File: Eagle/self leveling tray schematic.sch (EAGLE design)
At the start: 9 parts

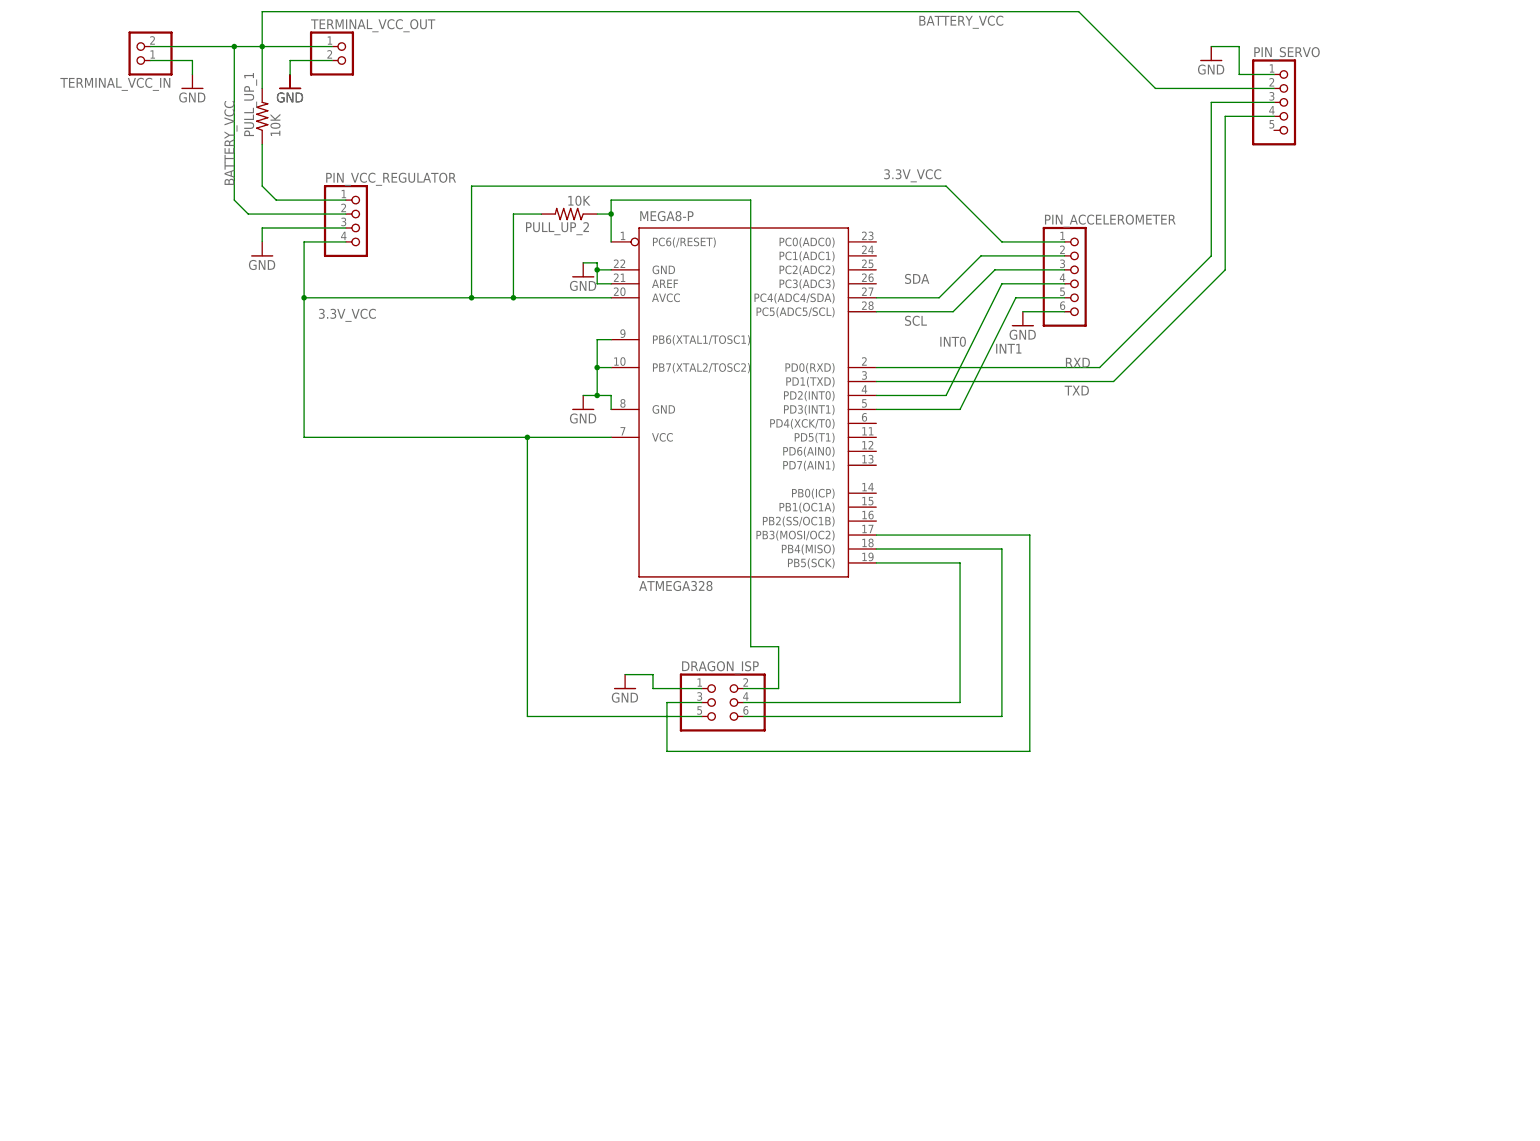
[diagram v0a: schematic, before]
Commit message: Schematic & Layout
Fixed ERC errors in schematic.
Created (practice?) layout.
Taylor Griffin
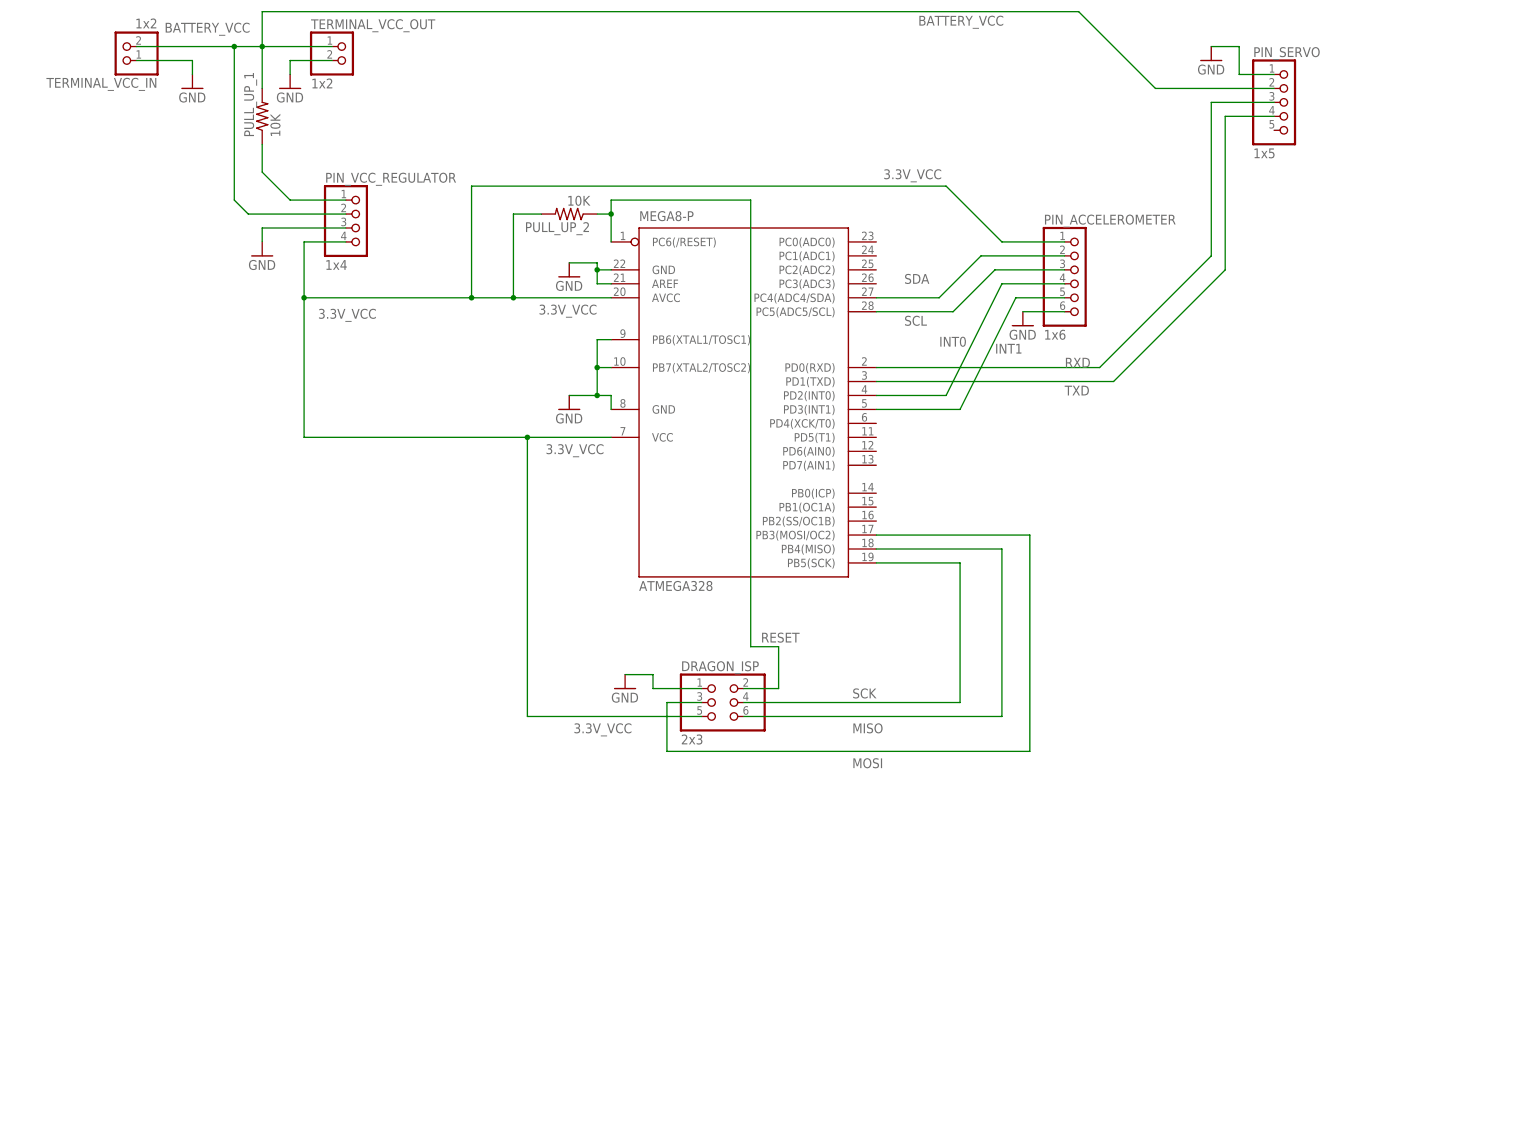
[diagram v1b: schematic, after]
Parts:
- DRAGON_ISP: value (none) -> 2x3
- PIN_ACCELEROMETER: value (none) -> 1x6
- PIN_SERVO: value (none) -> 1x5
- PIN_VCC_REGULATOR: value (none) -> 1x4
- TERMINAL_VCC_IN, TERMINAL_VCC_OUT: value (none) -> 1x2
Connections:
- net N$2 renamed MOSI
- net N$3 renamed MISO
- net N$4 renamed SCK
- net N$6 renamed RESET
- new net SHDN: PIN_VCC_REGULATOR.1, PULL_UP_1.1
- net BATTERY_VCC: no longer PIN_VCC_REGULATOR.1, PULL_UP_1.1
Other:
- moved on the sheet: TERMINAL_VCC_IN
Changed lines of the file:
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@@
 <part name="FRAME1" library="frames" deviceset="FRAME_A_L" device=""/>
 <part name="ATMEGA328" library="atmel" deviceset="MEGA8-P" device=""/>
-<part name="PIN_ACCELEROMETER" library="pinhead" deviceset="PINHD-1X6" device=""/>
-<part name="PIN_SERVO" library="pinhead" deviceset="PINHD-1X5" device=""/>
-<part name="PIN_VCC_REGULATOR" library="pinhead" deviceset="PINHD-1X4" device=""/>
-<part name="TERMINAL_VCC_IN" library="pinhead" deviceset="PINHD-1X2" device=""/>
-<part name="TERMINAL_VCC_OUT" library="pinhead" deviceset="PINHD-1X2" device=""/>
+<part name="PIN_ACCELEROMETER" library="pinhead" deviceset="PINHD-1X6" device="" value="1x6"/>
+<part name="PIN_SERVO" library="pinhead" deviceset="PINHD-1X5" device="" value="1x5"/>
+<part name="PIN_VCC_REGULATOR" library="pinhead" deviceset="PINHD-1X4" device="" value="1x4"/>
+<part name="TERMINAL_VCC_IN" library="pinhead" deviceset="PINHD-1X2" device="" value="1x2"/>
+<part name="TERMINAL_VCC_OUT" library="pinhead" deviceset="PINHD-1X2" device="" value="1x2"/>
 <part name="PULL_UP_1" library="rcl" deviceset="R-US_" device="M1206" value="10K"/>
 <part name="GND1" library="supply1" deviceset="GND" device=""/>
@@
 <part name="GND6" library="supply1" deviceset="GND" device=""/>
 <part name="PULL_UP_2" library="rcl" deviceset="R-US_" device="M1206" value="10K"/>
+<part name="GND4" library="supply1" deviceset="GND" device=""/>
+<part name="DRAGON_ISP" library="pinhead" deviceset="PINHD-2X3" device="" value="2x3"/>
+<part name="GND9" library="supply1" deviceset="GND" device=""/>
 <part name="GND7" library="supply1" deviceset="GND" device=""/>
-<part name="GND8" library="supply1" deviceset="GND" device=""/>
-<part name="GND4" library="supply1" deviceset="GND" device=""/>
-<part name="DRAGON_ISP" library="pinhead" deviceset="PINHD-2X3" device=""/>
-<part name="GND9" library="supply1" deviceset="GND" device=""/>
 </parts>
 <sheets>
@@
 <instance part="PIN_SERVO" gate="A" x="222.25" y="142.24"/>
 <instance part="PIN_VCC_REGULATOR" gate="A" x="53.34" y="119.38"/>
-<instance part="TERMINAL_VCC_IN" gate="G$1" x="12.7" y="152.4" rot="R180"/>
+<instance part="TERMINAL_VCC_IN" gate="G$1" x="10.16" y="152.4" rot="R180"/>
 <instance part="TERMINAL_VCC_OUT" gate="G$1" x="50.8" y="149.86"/>
 <instance part="PULL_UP_1" gate="G$1" x="35.56" y="139.7" rot="R90"/>
-<instance part="GND1" gate="1" x="93.98" y="86.36"/>
-<instance part="GND2" gate="1" x="93.98" y="110.49"/>
+<instance part="GND1" gate="1" x="91.44" y="86.36"/>
+<instance part="GND2" gate="1" x="91.44" y="110.49"/>
 <instance part="GND3" gate="1" x="173.99" y="101.6"/>
 <instance part="GND5" gate="1" x="35.56" y="114.3"/>
 <instance part="GND6" gate="1" x="22.86" y="144.78"/>
 <instance part="PULL_UP_2" gate="G$1" x="91.44" y="121.92" rot="R180"/>
-<instance part="GND7" gate="1" x="40.64" y="144.78"/>
-<instance part="GND8" gate="1" x="40.64" y="144.78"/>
 <instance part="GND4" gate="1" x="208.28" y="149.86"/>
 <instance part="DRAGON_ISP" gate="A" x="118.11" y="33.02"/>
 <instance part="GND9" gate="1" x="101.6" y="35.56"/>
+<instance part="GND7" gate="1" x="40.64" y="144.78"/>
 </instances>
 <busses>
@@
 <pinref part="TERMINAL_VCC_IN" gate="G$1" pin="2"/>
 <pinref part="TERMINAL_VCC_OUT" gate="G$1" pin="1"/>
-<wire x1="15.24" y1="152.4" x2="30.48" y2="152.4" width="0.1524" layer="91"/>
+<wire x1="12.7" y1="152.4" x2="30.48" y2="152.4" width="0.1524" layer="91"/>
 <junction x="30.48" y="152.4"/>
 <wire x1="30.48" y1="152.4" x2="35.56" y2="152.4" width="0.1524" layer="91"/>
@@
 <wire x1="35.56" y1="144.78" x2="35.56" y2="152.4" width="0.1524" layer="91"/>
 <junction x="35.56" y="152.4"/>
-<label x="30.48" y="127" size="1.778" layer="95" rot="R90"/>
 <pinref part="PULL_UP_1" gate="G$1" pin="2"/>
 <wire x1="35.56" y1="152.4" x2="35.56" y2="158.75" width="0.1524" layer="91"/>
@@
 <wire x1="198.12" y1="144.78" x2="219.71" y2="144.78" width="0.1524" layer="91"/>
 <label x="154.94" y="156.21" size="1.778" layer="95"/>
-</segment>
-<segment>
-<wire x1="35.56" y1="134.62" x2="35.56" y2="127" width="0.1524" layer="91"/>
-<wire x1="35.56" y1="127" x2="38.1" y2="124.46" width="0.1524" layer="91"/>
-<pinref part="PIN_VCC_REGULATOR" gate="A" pin="1"/>
-<wire x1="38.1" y1="124.46" x2="50.8" y2="124.46" width="0.1524" layer="91"/>
-<pinref part="PULL_UP_1" gate="G$1" pin="1"/>
+<label x="17.78" y="154.94" size="1.778" layer="95"/>
 </segment>
 </net>
@@
 <wire x1="83.82" y1="30.48" x2="83.82" y2="81.28" width="0.1524" layer="91"/>
 <junction x="83.82" y="81.28"/>
+<label x="102.87" y="29.21" size="1.778" layer="95" rot="R180"/>
+<label x="97.79" y="80.01" size="1.778" layer="95" rot="R180"/>
+<label x="96.52" y="105.41" size="1.778" layer="95" rot="R180"/>
 </segment>
 </net>
@@
 <segment>
 <pinref part="GND2" gate="1" pin="GND"/>
-<wire x1="96.52" y1="113.03" x2="93.98" y2="113.03" width="0.1524" layer="91"/>
+<wire x1="96.52" y1="113.03" x2="91.44" y2="113.03" width="0.1524" layer="91"/>
 <pinref part="ATMEGA328" gate="G$1" pin="AREF"/>
 <wire x1="99.06" y1="109.22" x2="96.52" y2="109.22" width="0.1524" layer="91"/>
@@
 <wire x1="99.06" y1="88.9" x2="96.52" y2="88.9" width="0.1524" layer="91"/>
 <pinref part="GND1" gate="1" pin="GND"/>
-<wire x1="96.52" y1="88.9" x2="93.98" y2="88.9" width="0.1524" layer="91"/>
+<wire x1="96.52" y1="88.9" x2="91.44" y2="88.9" width="0.1524" layer="91"/>
 <pinref part="ATMEGA328" gate="G$1" pin="PB6(XTAL1/TOSC1)"/>
 <wire x1="99.06" y1="99.06" x2="96.52" y2="99.06" width="0.1524" layer="91"/>
@@
 <segment>
 <pinref part="TERMINAL_VCC_IN" gate="G$1" pin="1"/>
-<wire x1="15.24" y1="149.86" x2="22.86" y2="149.86" width="0.1524" layer="91"/>
+<wire x1="12.7" y1="149.86" x2="22.86" y2="149.86" width="0.1524" layer="91"/>
 <wire x1="22.86" y1="149.86" x2="22.86" y2="147.32" width="0.1524" layer="91"/>
 <pinref part="GND6" gate="1" pin="GND"/>
@@
 <wire x1="181.61" y1="104.14" x2="173.99" y2="104.14" width="0.1524" layer="91"/>
 <pinref part="GND3" gate="1" pin="GND"/>
-</segment>
-<segment>
-<pinref part="GND7" gate="1" pin="GND"/>
-<pinref part="GND8" gate="1" pin="GND"/>
-<pinref part="TERMINAL_VCC_OUT" gate="G$1" pin="2"/>
-<wire x1="48.26" y1="149.86" x2="40.64" y2="149.86" width="0.1524" layer="91"/>
-<wire x1="40.64" y1="149.86" x2="40.64" y2="147.32" width="0.1524" layer="91"/>
 </segment>
 <segment>
@@
 <wire x1="106.68" y1="38.1" x2="101.6" y2="38.1" width="0.1524" layer="91"/>
 <pinref part="GND9" gate="1" pin="GND"/>
+</segment>
+<segment>
+<pinref part="TERMINAL_VCC_OUT" gate="G$1" pin="2"/>
+<wire x1="48.26" y1="149.86" x2="40.64" y2="149.86" width="0.1524" layer="91"/>
+<wire x1="40.64" y1="147.32" x2="40.64" y2="149.86" width="0.1524" layer="91"/>
+<pinref part="GND7" gate="1" pin="GND"/>
 </segment>
 </net>
@@
 </segment>
 </net>
-<net name="N$2" class="0">
+<net name="MOSI" class="0">
 <segment>
 <pinref part="ATMEGA328" gate="G$1" pin="PB3(MOSI/OC2)"/>
@@
 <wire x1="109.22" y1="24.13" x2="175.26" y2="24.13" width="0.1524" layer="91"/>
 <wire x1="175.26" y1="24.13" x2="175.26" y2="63.5" width="0.1524" layer="91"/>
-</segment>
-</net>
-<net name="N$3" class="0">
+<label x="148.59" y="22.86" size="1.778" layer="95" rot="R180"/>
+</segment>
+</net>
+<net name="MISO" class="0">
 <segment>
 <pinref part="ATMEGA328" gate="G$1" pin="PB4(MISO)"/>
@@
 <wire x1="123.19" y1="30.48" x2="170.18" y2="30.48" width="0.1524" layer="91"/>
 <wire x1="170.18" y1="30.48" x2="170.18" y2="60.96" width="0.1524" layer="91"/>
-</segment>
-</net>
-<net name="N$4" class="0">
+<label x="148.59" y="29.21" size="1.778" layer="95" rot="R180"/>
+</segment>
+</net>
+<net name="SCK" class="0">
 <segment>
 <pinref part="ATMEGA328" gate="G$1" pin="PB5(SCK)"/>
@@
 <wire x1="123.19" y1="33.02" x2="162.56" y2="33.02" width="0.1524" layer="91"/>
 <wire x1="162.56" y1="33.02" x2="162.56" y2="58.42" width="0.1524" layer="91"/>
-</segment>
-</net>
-<net name="N$6" class="0">
+<label x="147.32" y="35.56" size="1.778" layer="95" rot="R180"/>
+</segment>
+</net>
+<net name="RESET" class="0">
 <segment>
 <pinref part="PULL_UP_2" gate="G$1" pin="1"/>
@@
 <wire x1="129.54" y1="43.18" x2="129.54" y2="35.56" width="0.1524" layer="91"/>
 <wire x1="129.54" y1="35.56" x2="123.19" y2="35.56" width="0.1524" layer="91"/>
+<label x="133.35" y="45.72" size="1.778" layer="95" rot="R180"/>
+</segment>
+</net>
+<net name="SHDN" class="0">
+<segment>
+<pinref part="PULL_UP_1" gate="G$1" pin="1"/>
+<wire x1="35.56" y1="134.62" x2="35.56" y2="129.54" width="0.1524" layer="91"/>
+<pinref part="PIN_VCC_REGULATOR" gate="A" pin="1"/>
+<wire x1="35.56" y1="129.54" x2="40.64" y2="124.46" width="0.1524" layer="91"/>
+<wire x1="40.64" y1="124.46" x2="50.8" y2="124.46" width="0.1524" layer="91"/>
 </segment>
 </net>
@@
 </sheet>
 </sheets>
+<errors>
+</errors>
 </schematic>
 </drawing>

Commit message: Schematic Version 1.2
Added changes suggested by Andrew.
Added LEDs and grounded unused GPIO.

Email from Andrew:
Hi Taylor!

> Could you take a look at our current schematic? It passes ERC right
now,
> but I'm not sure if I'm missing something critical.

- You need 100 nF bypass caps on the 328's VCC and AVCC pins.
- Use a 3.3V supply symbol, not wires, for your supply.
- Your regulator absolutely needs filter caps - large filter caps. Read
the data sheet.
- What's your battery voltage? what kind of batteries? note it in the
schematic.
- What kind of accelerometer? Note it in the schermatic.
- No crystal, so you're using the internal RC oscilator
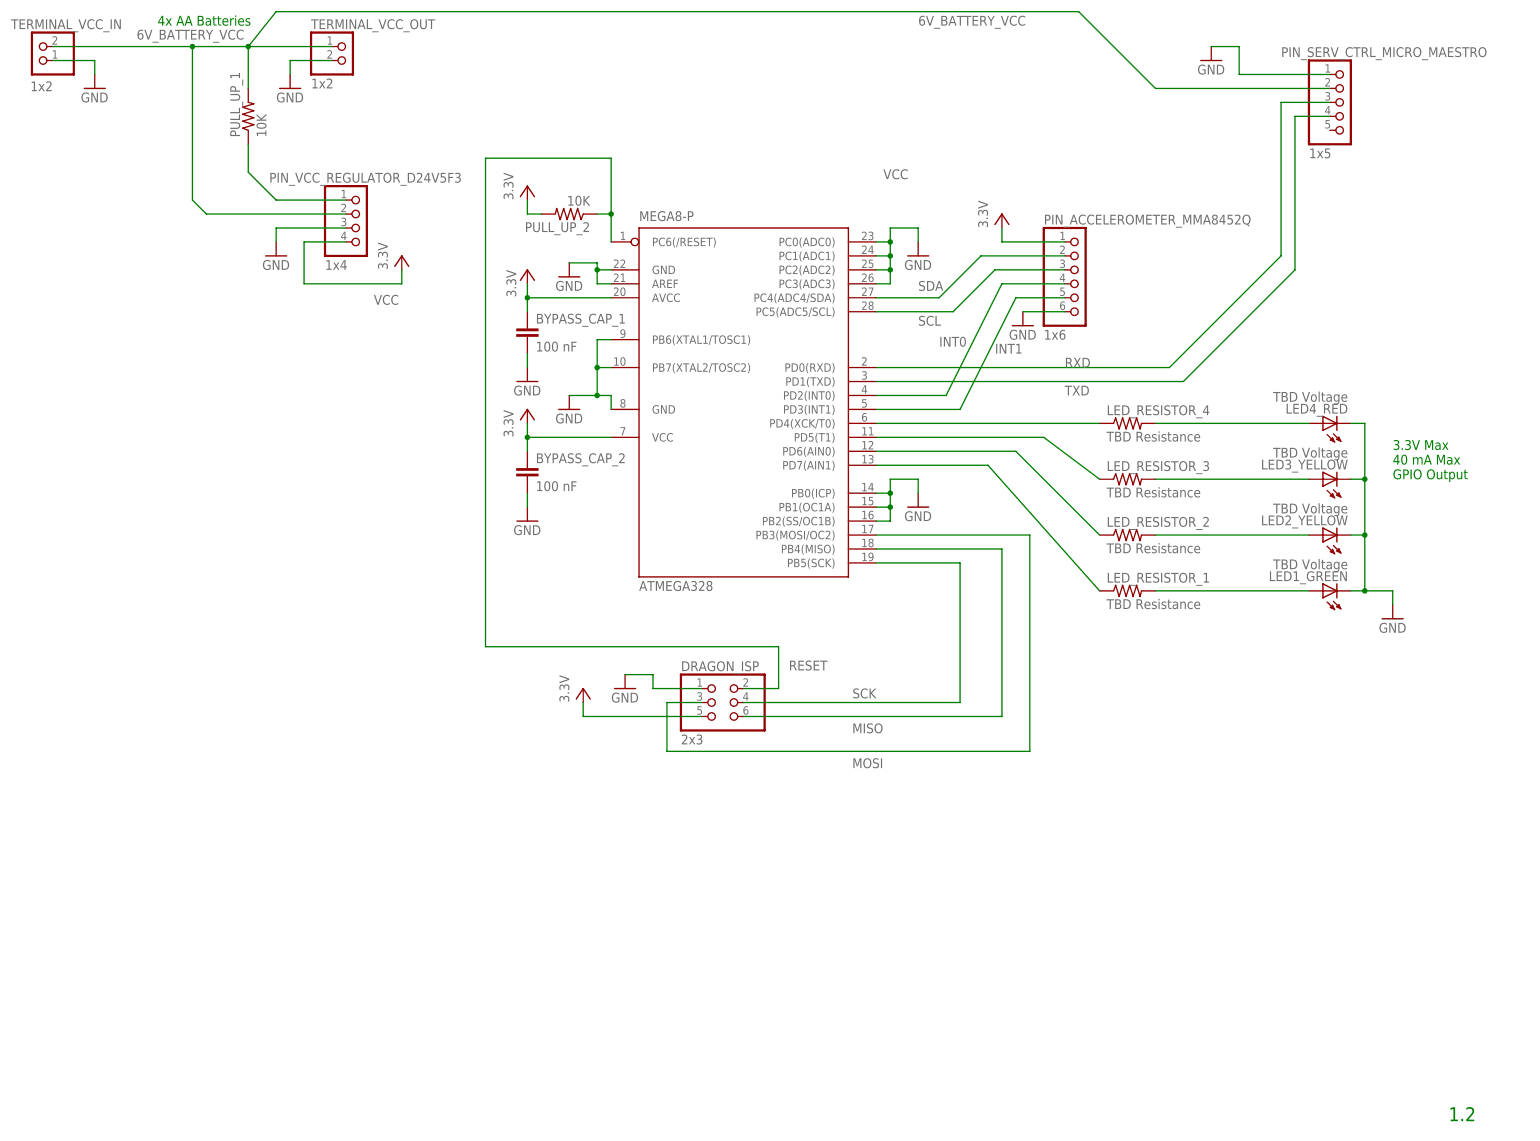
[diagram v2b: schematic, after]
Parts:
- removed PIN_SERVO: 1x5, pinhead:PINHD-1X5
- added BYPASS_CAP_1, BYPASS_CAP_2: 100 nF, rcl:C-EUC1206
- added LED1_GREEN, LED2_YELLOW, LED3_YELLOW, LED4_RED: TBD Voltage, led:LEDSMT1206
- added LED_RESISTOR_1, LED_RESISTOR_2, LED_RESISTOR_3, LED_RESISTOR_4: TBD Resistance, rcl:R-US_R1206
- added PIN_SERV_CTRL_MICRO_MAESTRO: 1x5, pinhead:PINHD-1X5
- renumbered PIN_ACCELEROMETER to PIN_ACCELEROMETER_MMA8452Q, PIN_VCC_REGULATOR to PIN_VCC_REGULATOR_D24V5F3
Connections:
- removed net 3.3V_VCC: ATMEGA328.AVCC, ATMEGA328.VCC@1, DRAGON_ISP.5, PIN_ACCELEROMETER_MMA8452Q.1, PIN_VCC_REGULATOR_D24V5F3.4, PULL_UP_2.2
- removed net BATTERY_VCC: PIN_SERVO.2, PIN_VCC_REGULATOR_D24V5F3.2, PULL_UP_1.2, TERMINAL_VCC_IN.2, TERMINAL_VCC_OUT.1
- new net 6V_BATTERY_VCC: PIN_SERV_CTRL_MICRO_MAESTRO.2, PIN_VCC_REGULATOR_D24V5F3.2, PULL_UP_1.2, TERMINAL_VCC_IN.2, TERMINAL_VCC_OUT.1
- new net LED_OUT_1: ATMEGA328.PD7(AIN1), LED_RESISTOR_1.1
- new net LED_OUT_2: ATMEGA328.PD6(AIN0), LED_RESISTOR_2.1
- new net LED_OUT_3: ATMEGA328.PD5(T1), LED_RESISTOR_3.1
- new net LED_OUT_4: ATMEGA328.PD4(XCK/T0), LED_RESISTOR_4.1
- new net N$2: LED1_GREEN.A, LED_RESISTOR_1.2
- new net N$3: LED2_YELLOW.A, LED_RESISTOR_2.2
- new net N$4: LED3_YELLOW.A, LED_RESISTOR_3.2
- new net N$5: LED4_RED.A, LED_RESISTOR_4.2
- new net VCC: ATMEGA328.AVCC, ATMEGA328.VCC@1, BYPASS_CAP_1.1, BYPASS_CAP_2.1, DRAGON_ISP.5, PIN_ACCELEROMETER_MMA8452Q.1, PIN_VCC_REGULATOR_D24V5F3.4, PULL_UP_2.2
- net GND: now also ATMEGA328.PB0(ICP), ATMEGA328.PB1(OC1A), ATMEGA328.PB2(SS/OC1B), ATMEGA328.PC0(ADC0), ATMEGA328.PC1(ADC1), ATMEGA328.PC2(ADC2), ATMEGA328.PC3(ADC3), BYPASS_CAP_1.2, BYPASS_CAP_2.2, LED1_GREEN.C, LED2_YELLOW.C, LED3_YELLOW.C, LED4_RED.C, PIN_SERV_CTRL_MICRO_MAESTRO.1; no longer PIN_SERVO.1
- net RXD: now also PIN_SERV_CTRL_MICRO_MAESTRO.3; no longer PIN_SERVO.3
- net TXD: now also PIN_SERV_CTRL_MICRO_MAESTRO.4; no longer PIN_SERVO.4
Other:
- note added: "1.2"
- note added: "3.3V Max 40 mA Max GPIO Output"
- note added: "4x AA Batteries"
- moved on the sheet: PULL_UP_1, TERMINAL_VCC_IN
